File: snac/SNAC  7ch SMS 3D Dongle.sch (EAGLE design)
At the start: 21 parts, among them IC1 4030D, IC2 4030D, K2 692112030100, Q9 BC849SMD, X2 STEREOJACK

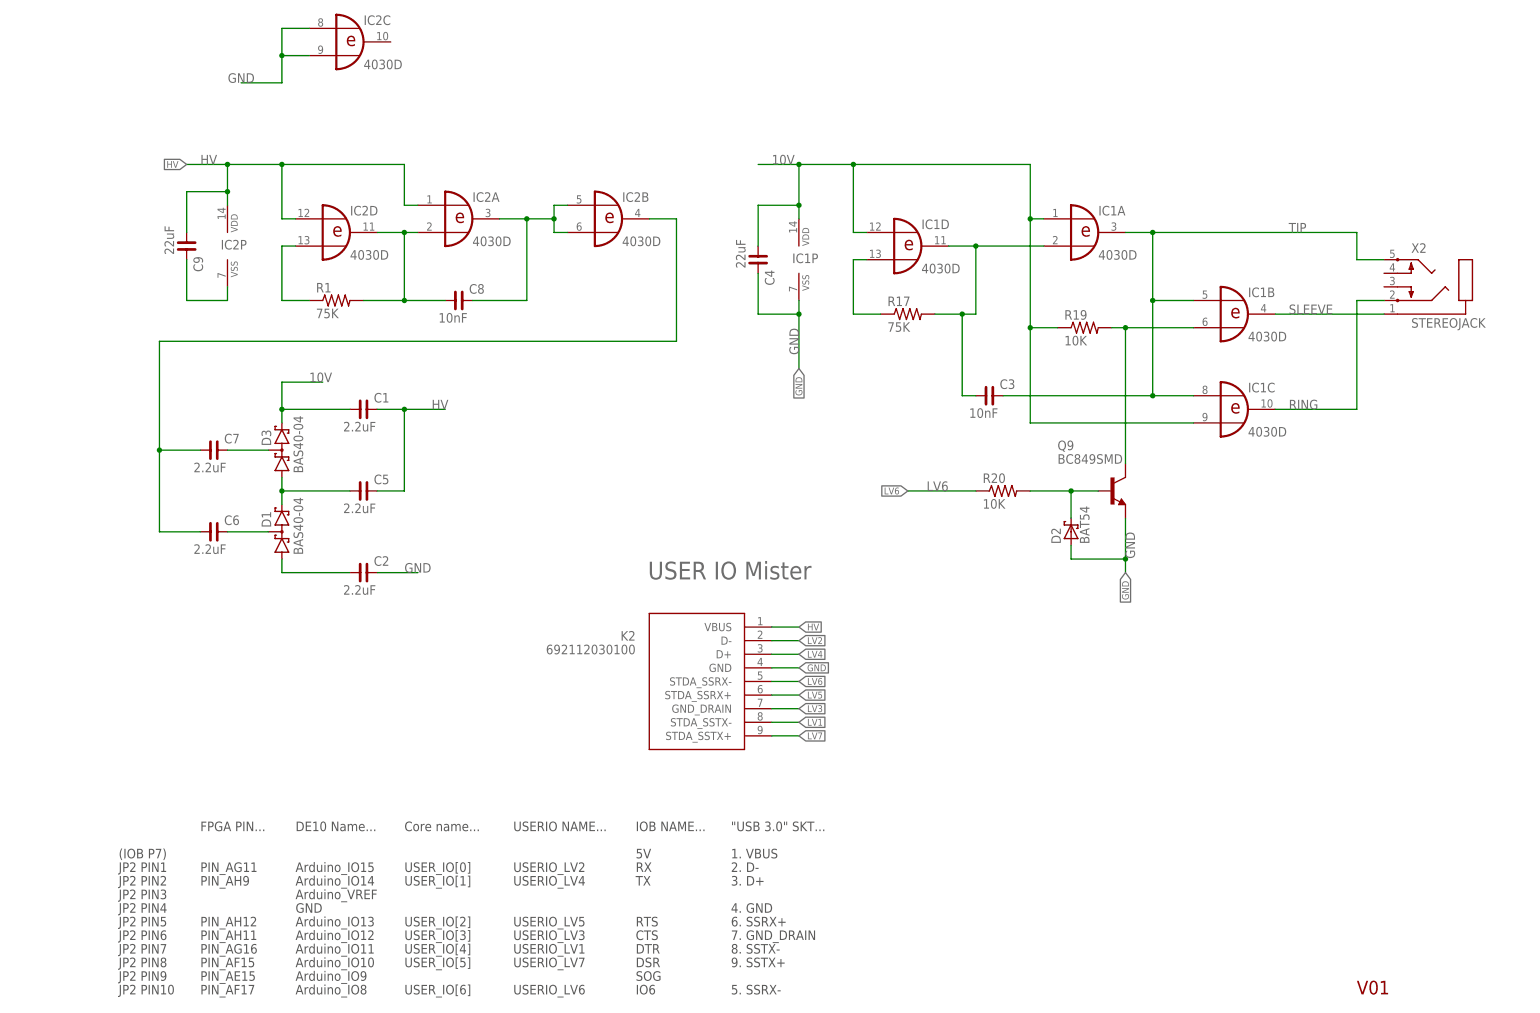
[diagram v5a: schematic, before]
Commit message: SMS 3D dongle charge pump and BOM updated
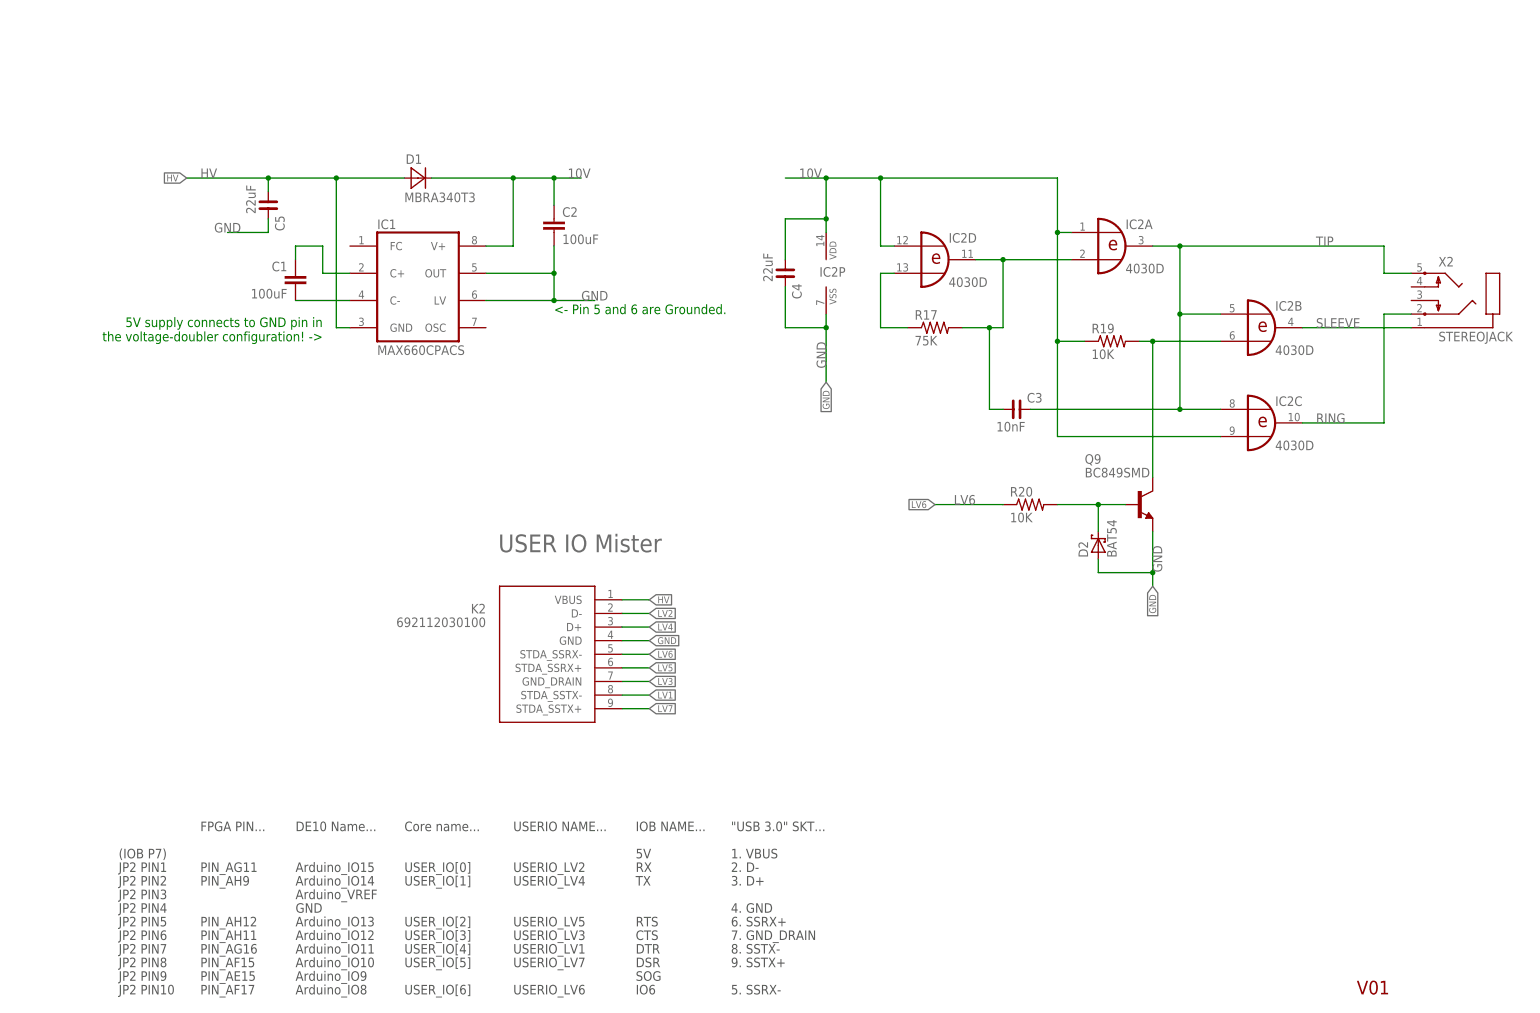
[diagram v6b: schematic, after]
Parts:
- removed C6, C7: 2.2uF, rc-master-smd:C_0805
- removed C8: 10nF, rc-master-smd:C_0805
- removed C9: 22uF, rc-master-smd:C_0805
- removed D3: BAS40-04, diode:BAS40-04
- removed R1: 75K, SparkFun:RESISTOR0603-RES
- C1, C2: value 2.2uF -> 100uF; device rc-master-smd:C_0805 -> rcl:C-EUC1210
- C5: value 2.2uF -> 22uF
- D1: value BAS40-04 -> MBRA340T3; device diode:BAS40-04 -> diode:MBRA340T3
- IC1: value 4030D -> MAX660CPACS; device 40xx:4030D -> maxim:MAX660CPACS
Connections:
- removed net N$11: C7.2, D3.C1A2
- removed net N$12: C6.2, D1.C1A2
- removed net N$16: C8.1, IC2A.I1, IC2D.O, R1.2
- removed net N$17: IC2D.I1, R1.1
- removed net N$6: C5.1, D1.C2, D3.A1
- removed net N$7: C6.1, C7.1, IC2B.O
- removed net N$8: C2.1, D1.A1
- removed net N$9: C8.2, IC2A.O, IC2B.I0, IC2B.I1
- new net N$25: C1.1, IC1.C+
- new net N$26: C1.2, IC1.C-
- net 10V: now also C2.1, D1.C, IC1.V+, IC2A.I0, IC2C.I1, IC2D.I0, IC2P.VDD; no longer C1.1, D3.C2, IC1A.I0, IC1C.I1, IC1D.I0, IC1P.VDD
- net GND: now also C5.2, IC1.LV, IC1.OUT; no longer C9.2, IC1P.VSS, IC2C.I0, IC2C.I1
- net HV: now also C5.1, D1.A, IC1.GND; no longer C1.2, C5.2, C9.1, IC2A.I0, IC2D.I0, IC2P.VDD
- net N$10: now also IC2D.I1; no longer IC1D.I1
- net N$13: now also IC2B.I1; no longer IC1B.I1
- net N$5: now also IC2A.I1, IC2D.O; no longer IC1A.I1, IC1D.O
- net RING: now also IC2C.O; no longer IC1C.O
- net SLEEVE: now also IC2B.O; no longer IC1B.O
- net TIP: now also IC2A.O, IC2B.I0, IC2C.I0; no longer IC1A.O, IC1B.I0, IC1C.I0
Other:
- note added: "5V supply connects to GND pin in the voltage-doubler configuration! ->"
- note added: "<- Pin 5 and 6 are Grounded."
- moved on the sheet: C1, C2, C3, C4, C5, D2, IC2A, IC2B, IC2C, IC2D, IC2P, K2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

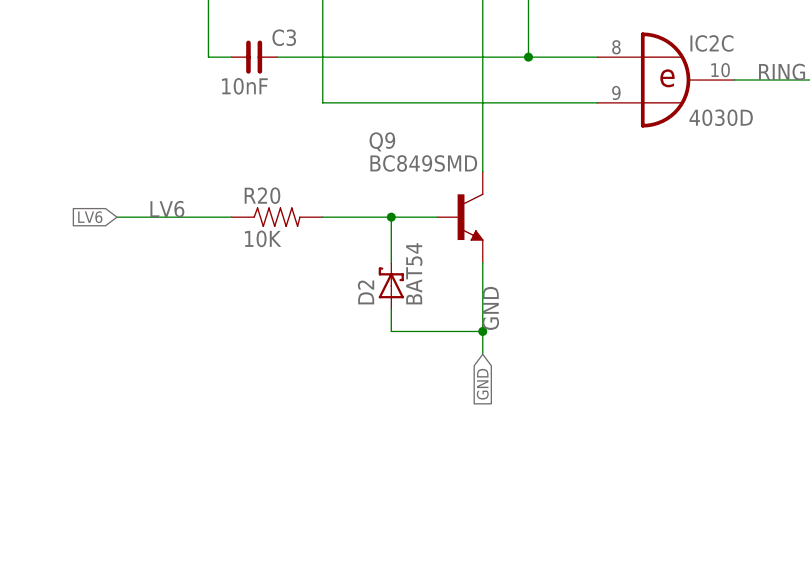
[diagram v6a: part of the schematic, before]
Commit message: Removed unneeded diode from the SMS 3D dongle + BOM
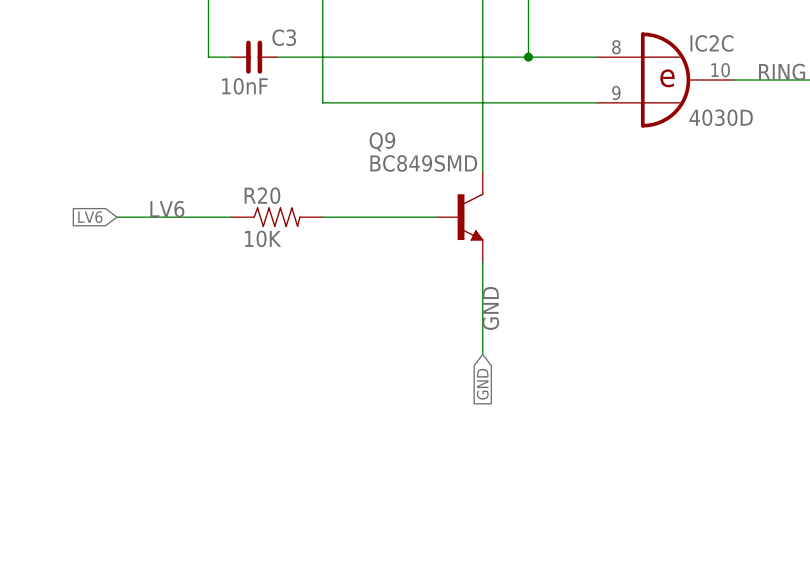
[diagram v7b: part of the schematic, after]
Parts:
- removed D2: BAT54, diode:BAT54
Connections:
- net GND: no longer D2.A
- net N$14: no longer D2.C
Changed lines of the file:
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@@
 <grid distance="0.1" unitdist="inch" unit="inch" style="lines" multiple="1" display="no" altdistance="0.01" altunitdist="inch" altunit="inch"/>
 <layers>
-<layer number="1" name="Top" color="4" fill="1" visible="yes" active="no"/>
-<layer number="2" name="Route2" color="1" fill="3" visible="yes" active="no"/>
-<layer number="3" name="Route3" color="4" fill="3" visible="yes" active="no"/>
-<layer number="4" name="Route4" color="1" fill="4" visible="yes" active="no"/>
-<layer number="5" name="Route5" color="4" fill="4" visible="yes" active="no"/>
-<layer number="6" name="Route6" color="1" fill="8" visible="yes" active="no"/>
-<layer number="7" name="Route7" color="4" fill="8" visible="yes" active="no"/>
-<layer number="8" name="Route8" color="1" fill="2" visible="yes" active="no"/>
-<layer number="9" name="Route9" color="4" fill="2" visible="yes" active="no"/>
-<layer number="10" name="Route10" color="1" fill="7" visible="yes" active="no"/>
-<layer number="11" name="Route11" color="4" fill="7" visible="yes" active="no"/>
-<layer number="12" name="Route12" color="1" fill="5" visible="yes" active="no"/>
-<layer number="13" name="Route13" color="4" fill="5" visible="yes" active="no"/>
-<layer number="14" name="Route14" color="1" fill="6" visible="yes" active="no"/>
-<layer number="15" name="Route15" color="4" fill="6" visible="yes" active="no"/>
-<layer number="16" name="Bottom" color="1" fill="1" visible="yes" active="no"/>
-<layer number="17" name="Pads" color="2" fill="1" visible="yes" active="no"/>
-<layer number="18" name="Vias" color="2" fill="1" visible="yes" active="no"/>
-<layer number="19" name="Unrouted" color="11" fill="1" visible="yes" active="no"/>
-<layer number="20" name="Dimension" color="6" fill="1" visible="yes" active="no"/>
-<layer number="21" name="tPlace" color="16" fill="1" visible="yes" active="no"/>
-<layer number="22" name="bPlace" color="14" fill="1" visible="yes" active="no"/>
-<layer number="23" name="tOrigins" color="15" fill="1" visible="yes" active="no"/>
-<layer number="24" name="bOrigins" color="15" fill="1" visible="yes" active="no"/>
-<layer number="25" name="tNames" color="7" fill="1" visible="yes" active="no"/>
-<layer number="26" name="bNames" color="7" fill="1" visible="yes" active="no"/>
-<layer number="27" name="tValues" color="12" fill="1" visible="yes" active="no"/>
-<layer number="28" name="bValues" color="7" fill="1" visible="yes" active="no"/>
+<layer number="1" name="Top" color="4" fill="1" visible="no" active="no"/>
+<layer number="2" name="Route2" color="1" fill="3" visible="no" active="no"/>
+<layer number="3" name="Route3" color="4" fill="3" visible="no" active="no"/>
+<layer number="4" name="Route4" color="1" fill="4" visible="no" active="no"/>
+<layer number="5" name="Route5" color="4" fill="4" visible="no" active="no"/>
+<layer number="6" name="Route6" color="1" fill="8" visible="no" active="no"/>
+<layer number="7" name="Route7" color="4" fill="8" visible="no" active="no"/>
+<layer number="8" name="Route8" color="1" fill="2" visible="no" active="no"/>
+<layer number="9" name="Route9" color="4" fill="2" visible="no" active="no"/>
+<layer number="10" name="Route10" color="1" fill="7" visible="no" active="no"/>
+<layer number="11" name="Route11" color="4" fill="7" visible="no" active="no"/>
+<layer number="12" name="Route12" color="1" fill="5" visible="no" active="no"/>
+<layer number="13" name="Route13" color="4" fill="5" visible="no" active="no"/>
+<layer number="14" name="Route14" color="1" fill="6" visible="no" active="no"/>
+<layer number="15" name="Route15" color="4" fill="6" visible="no" active="no"/>
+<layer number="16" name="Bottom" color="1" fill="1" visible="no" active="no"/>
+<layer number="17" name="Pads" color="2" fill="1" visible="no" active="no"/>
+<layer number="18" name="Vias" color="2" fill="1" visible="no" active="no"/>
+<layer number="19" name="Unrouted" color="11" fill="1" visible="no" active="no"/>
+<layer number="20" name="Dimension" color="6" fill="1" visible="no" active="no"/>
+<layer number="21" name="tPlace" color="16" fill="1" visible="no" active="no"/>
+<layer number="22" name="bPlace" color="14" fill="1" visible="no" active="no"/>
+<layer number="23" name="tOrigins" color="15" fill="1" visible="no" active="no"/>
+<layer number="24" name="bOrigins" color="15" fill="1" visible="no" active="no"/>
+<layer number="25" name="tNames" color="7" fill="1" visible="no" active="no"/>
+<layer number="26" name="bNames" color="7" fill="1" visible="no" active="no"/>
+<layer number="27" name="tValues" color="12" fill="1" visible="no" active="no"/>
+<layer number="28" name="bValues" color="7" fill="1" visible="no" active="no"/>
 <layer number="29" name="tStop" color="7" fill="3" visible="no" active="no"/>
 <layer number="30" name="bStop" color="7" fill="6" visible="no" active="no"/>
@@
 <layer number="35" name="tGlue" color="7" fill="4" visible="no" active="no"/>
 <layer number="36" name="bGlue" color="7" fill="5" visible="no" active="no"/>
-<layer number="37" name="tTest" color="7" fill="1" visible="yes" active="no"/>
-<layer number="38" name="bTest" color="7" fill="1" visible="yes" active="no"/>
+<layer number="37" name="tTest" color="7" fill="1" visible="no" active="no"/>
+<layer number="38" name="bTest" color="7" fill="1" visible="no" active="no"/>
 <layer number="39" name="tKeepout" color="4" fill="11" visible="no" active="no"/>
 <layer number="40" name="bKeepout" color="1" fill="11" visible="no" active="no"/>
@@
 <layer number="44" name="Drills" color="7" fill="1" visible="no" active="no"/>
 <layer number="45" name="Holes" color="7" fill="1" visible="no" active="no"/>
-<layer number="46" name="Milling" color="3" fill="1" visible="yes" active="no"/>
-<layer number="47" name="Measures" color="7" fill="1" visible="yes" active="no"/>
-<layer number="48" name="Document" color="7" fill="1" visible="yes" active="no"/>
-<layer number="49" name="Reference" color="7" fill="1" visible="yes" active="no"/>
-<layer number="50" name="dxf" color="7" fill="1" visible="yes" active="no"/>
-<layer number="51" name="tDocu" color="6" fill="1" visible="yes" active="no"/>
-<layer number="52" name="bDocu" color="7" fill="1" visible="yes" active="no"/>
-<layer number="53" name="tGND_GNDA" color="7" fill="9" visible="yes" active="no"/>
-<layer number="54" name="bGND_GNDA" color="1" fill="9" visible="yes" active="no"/>
-<layer number="56" name="wert" color="7" fill="1" visible="yes" active="no"/>
-<layer number="57" name="tCAD" color="7" fill="1" visible="yes" active="no"/>
-<layer number="59" name="tCarbon" color="7" fill="1" visible="yes" active="no"/>
-<layer number="60" name="bCarbon" color="7" fill="1" visible="yes" active="no"/>
+<layer number="46" name="Milling" color="3" fill="1" visible="no" active="no"/>
+<layer number="47" name="Measures" color="7" fill="1" visible="no" active="no"/>
+<layer number="48" name="Document" color="7" fill="1" visible="no" active="no"/>
+<layer number="49" name="Reference" color="7" fill="1" visible="no" active="no"/>
+<layer number="50" name="dxf" color="7" fill="1" visible="no" active="no"/>
+<layer number="51" name="tDocu" color="6" fill="1" visible="no" active="no"/>
+<layer number="52" name="bDocu" color="7" fill="1" visible="no" active="no"/>
+<layer number="53" name="tGND_GNDA" color="7" fill="9" visible="no" active="no"/>
+<layer number="54" name="bGND_GNDA" color="1" fill="9" visible="no" active="no"/>
+<layer number="56" name="wert" color="7" fill="1" visible="no" active="no"/>
+<layer number="57" name="tCAD" color="7" fill="1" visible="no" active="no"/>
+<layer number="59" name="tCarbon" color="7" fill="1" visible="no" active="no"/>
+<layer number="60" name="bCarbon" color="7" fill="1" visible="no" active="no"/>
 <layer number="88" name="SimResults" color="9" fill="1" visible="no" active="yes"/>
 <layer number="89" name="SimProbes" color="9" fill="1" visible="no" active="yes"/>
@@
 <part name="R19" library="SparkFun" deviceset="RESISTOR" device="0603-RES" value="10K"/>
 <part name="R20" library="SparkFun" deviceset="RESISTOR" device="0603-RES" value="10K"/>
-<part name="D2" library="diode" library_urn="urn:adsk.eagle:library:210" deviceset="BAT54" device="" package3d_urn="urn:adsk.eagle:package:43389/2"/>
 <part name="C4" library="rc-master-smd" deviceset="C_" device="0805" value="22uF"/>
 <part name="X2" library="adafruit" deviceset="STEREOJACK" device=""/>
@@
 <instance part="R19" gate="G$1" x="195.58" y="170.18"/>
 <instance part="R20" gate="G$1" x="180.34" y="139.7"/>
-<instance part="D2" gate="G$1" x="193.04" y="132.08" rot="R90"/>
 <instance part="C4" gate="G$1" x="134.62" y="182.88" rot="R270"/>
 <instance part="X2" gate="1" x="264.16" y="180.34"/>
@@
 <segment>
 <pinref part="Q9" gate="G$1" pin="E"/>
-<wire x1="203.2" y1="134.62" x2="203.2" y2="127" width="0.1524" layer="91"/>
+<wire x1="203.2" y1="134.62" x2="203.2" y2="124.46" width="0.1524" layer="91"/>
 <label x="203.2" y="132.08" size="1.778" layer="95" rot="R270"/>
-<pinref part="D2" gate="G$1" pin="A"/>
-<wire x1="203.2" y1="127" x2="203.2" y2="124.46" width="0.1524" layer="91"/>
-<wire x1="193.04" y1="129.54" x2="193.04" y2="127" width="0.1524" layer="91"/>
-<wire x1="193.04" y1="127" x2="203.2" y2="127" width="0.1524" layer="91"/>
-<junction x="203.2" y="127"/>
 </segment>
 <segment>
@@
 <pinref part="R20" gate="G$1" pin="2"/>
 <pinref part="Q9" gate="G$1" pin="B"/>
-<wire x1="185.42" y1="139.7" x2="193.04" y2="139.7" width="0.1524" layer="91"/>
-<pinref part="D2" gate="G$1" pin="C"/>
-<wire x1="193.04" y1="139.7" x2="198.12" y2="139.7" width="0.1524" layer="91"/>
-<wire x1="193.04" y1="134.62" x2="193.04" y2="139.7" width="0.1524" layer="91"/>
-<junction x="193.04" y="139.7"/>
-</segment>
-</net>
+<wire x1="185.42" y1="139.7" x2="198.12" y2="139.7" width="0.1524" layer="91"/>
+</segment>
+</net>
